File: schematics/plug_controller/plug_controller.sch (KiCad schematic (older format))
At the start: 20 parts, among them J1 Conn_01x04, J2 Conn_01x01, J3 Conn_01x01, J4 Conn_01x01, J5 Conn_01x01, Q1 MMBT3904L, Q2 MMBT3904L, Q3 MMBT3904L, Q4 MMBT3904L, U1 MOC3063M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

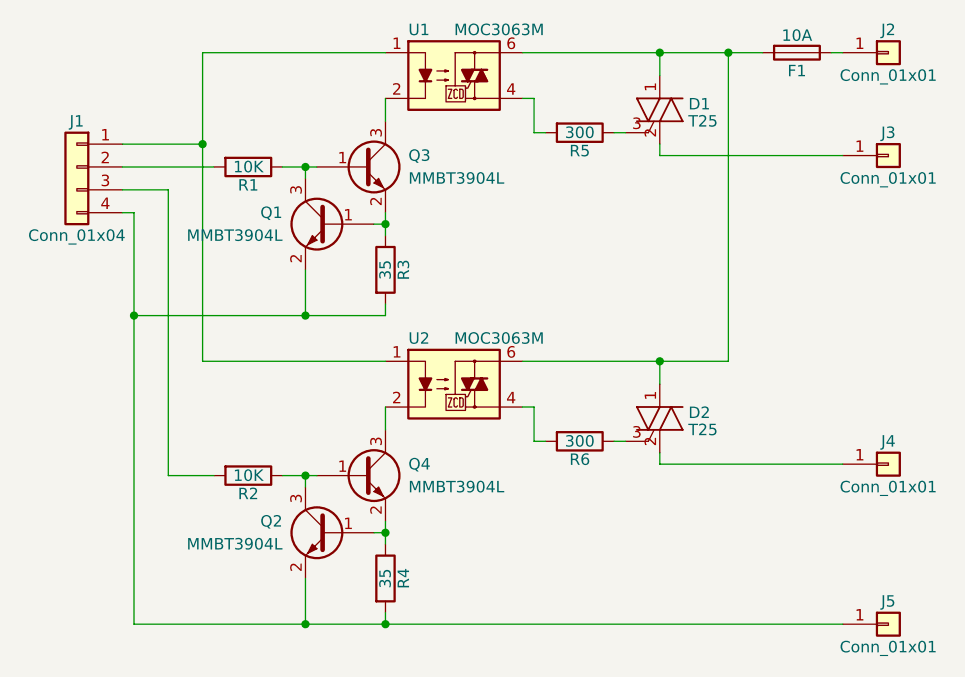
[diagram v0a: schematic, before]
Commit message: update footprints as assembling first design.
The triac pins were reversed.
The fuse footprints were not the holders i have.
The resistor between optotriac and triac should be larger.
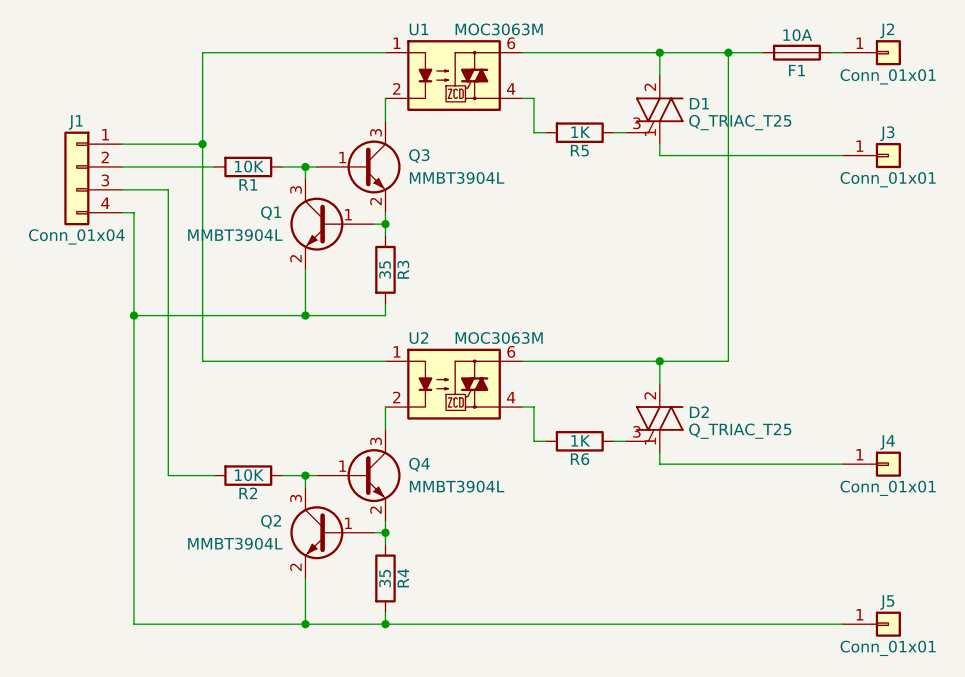
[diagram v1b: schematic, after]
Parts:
- removed D1, D2: T25, Local:D2PAK, symbol Q_TRIAC_AAG
- added D1, D2: Q_TRIAC_T25, Local:D2PAK, symbol Q_TRIAC_T25
- F1: footprint Fuse_Holders_and_Fuses:Fuseholder5x20_horiz_open_inline_Type-I -> Fuse_Holders_and_Fuses:Fuseholder5x20_horiz_open_lateral_Type-II
- R5, R6: value 300 -> 1K
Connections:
- net at F1.2, U1.6, U2.6: now also D1.2 (A1), D2.2 (A1)
- net at J3.1 (Pin_1): now also D1.1 (A2)
- net at R5.1: now also D1.3 (G)
- net at R6.1: now also D2.3 (G)
- net at J4.1 (Pin_1): now also D2.1 (A2)
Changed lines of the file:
@@
 LIBS:valves
 LIBS:dk_Thyristors-TRIACs
+LIBS:local
 LIBS:plug_controller-cache
 EELAYER 25 0
@@
 $EndDescr
 $Comp
-L Q_TRIAC_AAG D1
-U 1 1 5AD22718
-P 3300 1850
-F 0 "D1" H 3425 1875 50  0000 L CNN
-F 1 "T25" H 3425 1800 50  0000 L CNN
-F 2 "Local:D2PAK" V 3375 1875 50  0001 C CNN
-F 3 "" V 3300 1850 50  0001 C CNN
-	1    3300 1850
-	1    0    0    -1
-$EndComp
-$Comp
 L R R5
 U 1 1 5AD227DF
 P 2950 1950
 F 0 "R5" V 3030 1950 50  0000 C CNN
-F 1 "300" V 2950 1950 50  0000 C CNN
+F 1 "1K" V 2950 1950 50  0000 C CNN
 F 2 "Resistors_SMD:R_0603" V 2880 1950 50  0001 C CNN
 F 3 "" H 2950 1950 50  0001 C CNN
@@
 F 0 "F1" V 3980 1600 50  0000 C CNN
 F 1 "10A" V 3825 1600 50  0000 C CNN
-F 2 "Fuse_Holders_and_Fuses:Fuseholder5x20_horiz_open_inline_Type-I" V 3830 1600 50  0001 C CNN
+F 2 "Fuse_Holders_and_Fuses:Fuseholder5x20_horiz_open_lateral_Type-II" V 3830 1600 50  0001 C CNN
 F 3 "" H 3900 1600 50  0001 C CNN
 	1    3900 1600
@@
 P 2950 3300
 F 0 "R6" V 3030 3300 50  0000 C CNN
-F 1 "300" V 2950 3300 50  0000 C CNN
+F 1 "1K" V 2950 3300 50  0000 C CNN
 F 2 "Resistors_SMD:R_0603" V 2880 3300 50  0001 C CNN
 F 3 "" H 2950 3300 50  0001 C CNN
 	1    2950 3300
 	0    1    1    0
-$EndComp
-$Comp
-L Q_TRIAC_AAG D2
-U 1 1 5AD26CCE
-P 3300 3200
-F 0 "D2" H 3425 3225 50  0000 L CNN
-F 1 "T25" H 3425 3150 50  0000 L CNN
-F 2 "Local:D2PAK" V 3375 3225 50  0001 C CNN
-F 3 "" V 3300 3200 50  0001 C CNN
-	1    3300 3200
-	1    0    0    -1
 $EndComp
 Wire Wire Line
@@
 $EndComp
 Connection ~ 2100 4100
+$Comp
+L Q_TRIAC_T25 D1
+U 1 1 5AE49474
+P 3300 1850
+F 0 "D1" H 3425 1875 50  0000 L CNN
+F 1 "Q_TRIAC_T25" H 3425 1800 50  0000 L CNN
+F 2 "Local:D2PAK" V 3375 1875 50  0001 C CNN
+F 3 "" V 3300 1850 50  0001 C CNN
+	1    3300 1850
+	1    0    0    -1
+$EndComp
+$Comp
+L Q_TRIAC_T25 D2
+U 1 1 5AE495CB
+P 3300 3200
+F 0 "D2" H 3425 3225 50  0000 L CNN
+F 1 "Q_TRIAC_T25" H 3425 3150 50  0000 L CNN
+F 2 "Local:D2PAK" V 3375 3225 50  0001 C CNN
+F 3 "" V 3300 3200 50  0001 C CNN
+	1    3300 3200
+	1    0    0    -1
+$EndComp
 $EndSCHEMATC
